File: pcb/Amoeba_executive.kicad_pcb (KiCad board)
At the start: 2 copper layers, 19 x 19.1 mm, 4 parts, among them J1 Conn_01x04_MountingPin, J2 Conn_01x04_MountingPin, SW1 SW_PUSH_LED

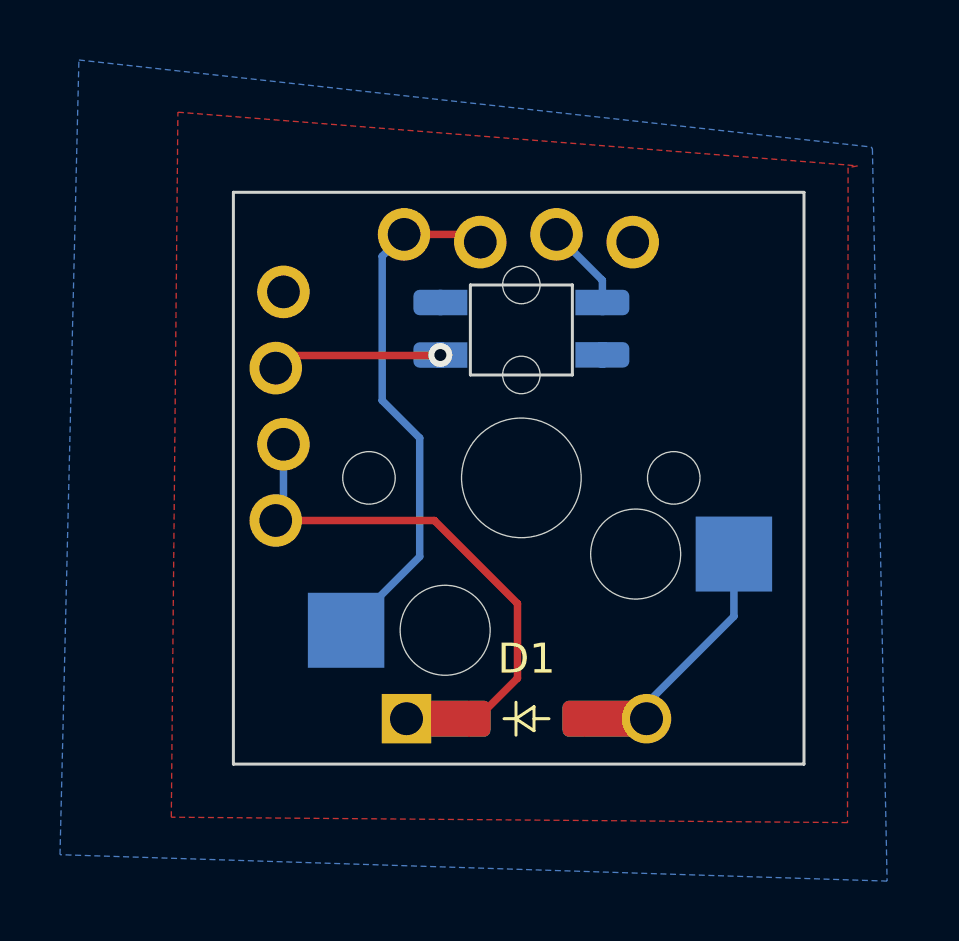
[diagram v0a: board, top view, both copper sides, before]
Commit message: two sets of 5 pins
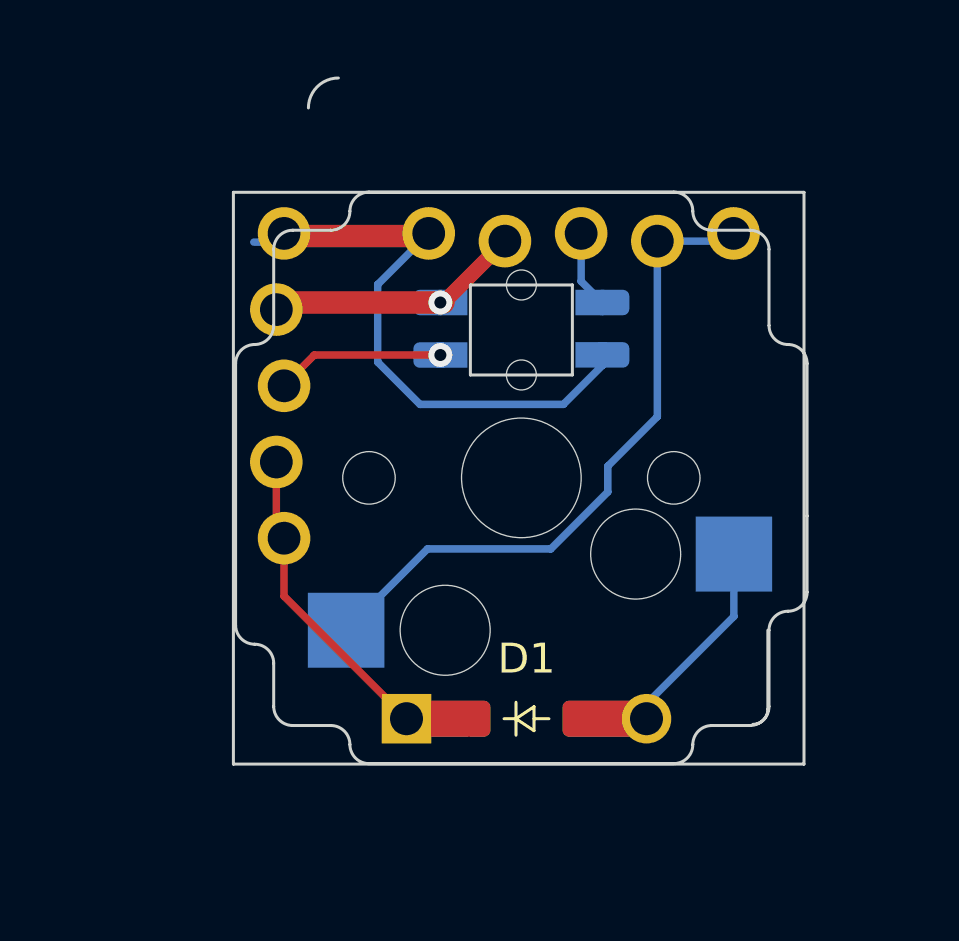
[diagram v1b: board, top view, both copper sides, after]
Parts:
- J1, J2: footprint ergodonk_kicad_library:amoeba_executive_4pinn_conn -> ergodonk_kicad_library:amoeba_executive_5pinn_conn
- SW1: footprint ergodonk_kicad_library:amoeba_executive_V2 -> ergodonk_kicad_library:amoeba_executive_V4
- moved J1 2.09 mm to (183.7, 77.4), turned to 0 degrees
- moved J2 0.68 mm to (173.7, 82.3), turned to -90 degrees
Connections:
- J1 pad 2: Net-(J1-Pin_2) -> VDD
- J1 pad 3: /Column -> Net-(J1-Pin_3)
- J2 pad 1: /Row -> GND
- J2 pad 2: /Row -> VDD
- J2 pad 4: VDD -> /Row
- SW1 pad 4: Net-(J1-Pin_2) -> Net-(J1-Pin_3)
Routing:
- net GND: track 0.73 -> 19.7 mm
- net VDD: track 0.00 -> 8.66 mm, vias 0 -> 1
- net /Column: track 17.7 -> 23.4 mm
- net /Row: track 16.2 -> 10.9 mm
- net Net-(J1-Pin_2): track 2.90 -> 0.00 mm
- net Net-(J1-Pin_3): track 0.00 -> 2.82 mm
- removed copper zone on B.Cu, net GND
- removed copper zone on F.Cu, net VDD
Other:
- board size 19 x 19.1 mm -> 19 x 22.9 mm

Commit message: First draft complete
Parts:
- added REF**: Amoeba_MountingHole_2.2mm_M2_DIN965_Pad_TopOnly, ergodonk_kicad_library:Amoeba_MountingHole_2.2mm_M2_DIN965_Pad_TopOnly, F.Cu at (189.8, 93.5)
- added REF**: 2.54 gird, ergodonk_kicad_library:2.54 gird, F.Cu at (178.7, 86.5)
- moved D1 4.36 mm to (177.5, 93.4), turned to 180 degrees
- moved J2 0.30 mm to (173.5, 82.1)
- moved J1 0.23 mm to (183.7, 77.1)
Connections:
- D1 pad 1: /Row -> Net-(D1-K)
- D1 pad 2: Net-(D1-A) -> /Row
- SW1 pad 5: Net-(D1-A) -> Net-(D1-K)
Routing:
- net Net-(D1-K): track 0.00 -> 9.55 mm
- net Net-(D1-A): track 6.70 -> 0.00 mm
- net /Row: track 10.9 -> 9.83 mm
- net GND: track 19.7 -> 20.6 mm
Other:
- board size 19 x 22.9 mm -> 19.1 x 19 mm

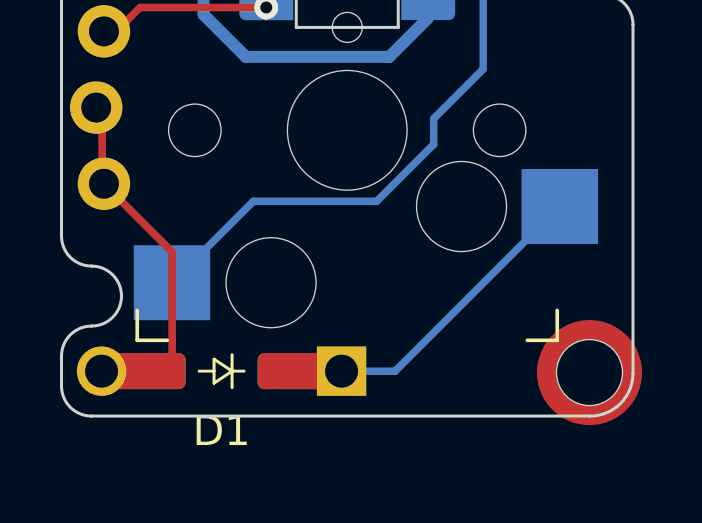
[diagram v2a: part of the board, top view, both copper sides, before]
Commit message: Created footprint library consolidated footprints in new library adjusted pads for single sided diodes
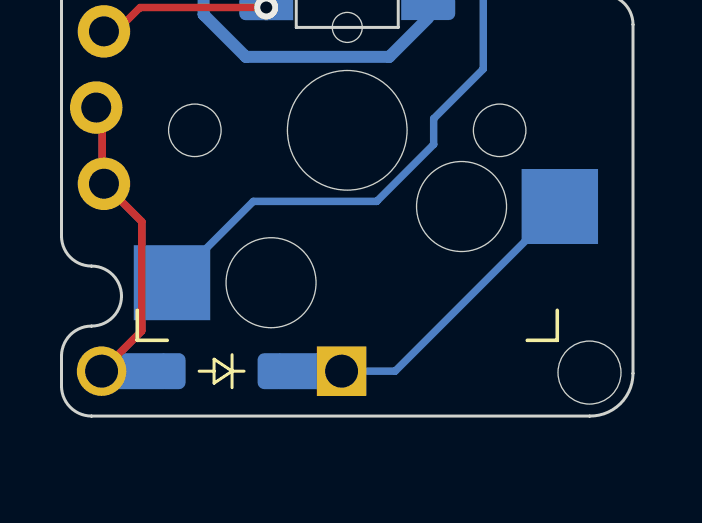
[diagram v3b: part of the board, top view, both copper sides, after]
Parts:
- D1: footprint ergodonk_kicad_library:D_SOD-123_DO-35_Hybrid_DoubleSided -> Amoeba_executive_footprints:D_SOD-123_DO-35_Hybrid_Single_sided; moved to B.Cu
- J1, J2: footprint ergodonk_kicad_library:amoeba_executive_5pinn_conn -> Amoeba_executive_footprints:amoeba_executive_5pinn_conn
- REF**: footprint ergodonk_kicad_library:Amoeba_MountingHole_2.2mm_M2_DIN965_Pad_TopOnly -> Amoeba_executive_footprints:Amoeba_MountingHole_2.2mm_M2_DIN965_Pad_TopOnly
- SW1: footprint ergodonk_kicad_library:amoeba_executive_V4 -> Amoeba_executive_footprints:amoeba_executive_V4
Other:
- board text added: "COLUMNS"
- board text added: "GND"
- board text added: "LED IN"
- board text added: "LED OUT"
- board text added: "ROWS"
- board text added: "VDD"

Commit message: SENT OUT FOR PRODUCTION Added basic branding Generated gerbers
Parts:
- added Amoeba-Logo-Small: G***, Amoeba_executive_footprints:amoeba-logo-small, F.Cu at (189.5, 85.0)
- added Amoeba-Logo-Small: G***, Amoeba_executive_footprints:amoeba-logo-small, B.Cu at (189.5, 85.0)
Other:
- board text added: "AMOEBA KingPin v0.1"
- board text added: "GND -"
- board text added: "VDD +"
